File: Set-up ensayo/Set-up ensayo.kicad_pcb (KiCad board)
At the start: 2 copper layers, 14 parts, among them J1 Conn_Coaxial, J2 DB9_Female_MountingHoles

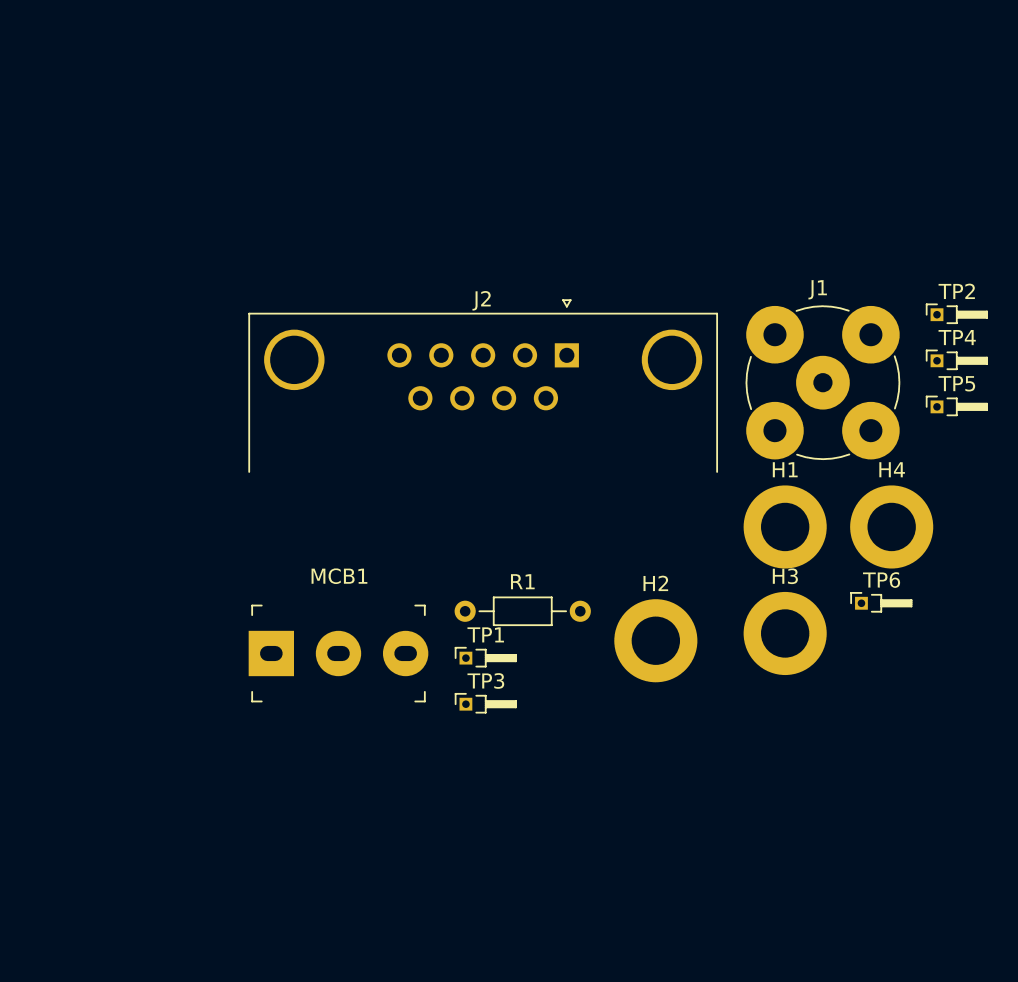
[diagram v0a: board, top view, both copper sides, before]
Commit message: Agregado de footprint de potenciómetro a PCB
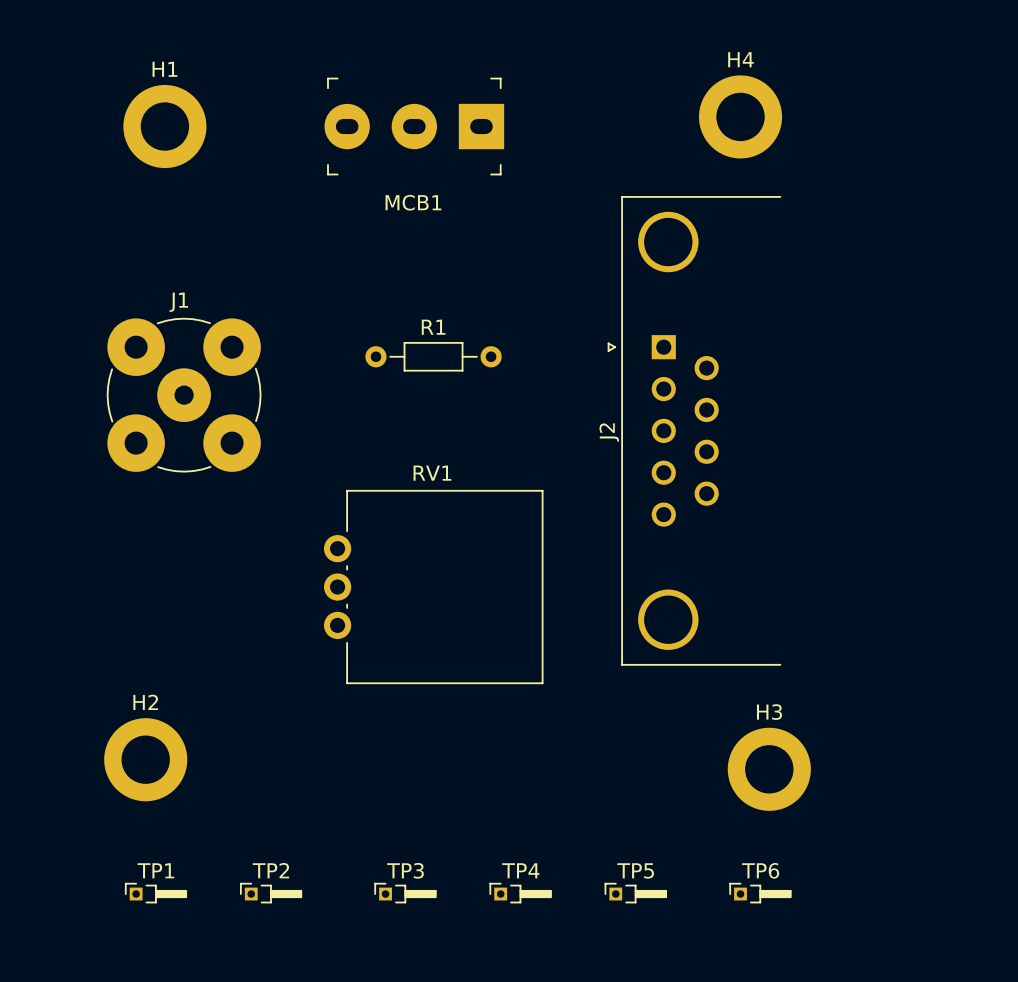
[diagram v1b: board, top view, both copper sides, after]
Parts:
- added RV1: R_POT, Footprints proyecto:Potentiometer_Vishay_248GJ-249GJ_Single_Vertical, F.Cu at (116.8, 114.3)
- moved TP2 59.4 mm to (111.1, 132.1)
- moved H1 48.9 mm to (105.4, 81.3)
- moved TP4 45.6 mm to (127.6, 132.1)
- moved J1 42.3 mm to (106.7, 99.1)
- moved TP5 38.6 mm to (135.3, 132.1)
- moved MCB1 35.2 mm to (121.9, 81.3), turned to 180 degrees
- moved H2 34.7 mm to (104.1, 123.2)
- moved H4 28.9 mm to (143.5, 80.6)
- moved TP1 26.8 mm to (103.5, 132.1)
- moved TP6 20.8 mm to (143.5, 132.1)
- moved R1 17.9 mm to (119.4, 96.5)
- moved TP3 13.6 mm to (120.0, 132.1)
- moved H3 9.05 mm to (145.4, 123.8)
- moved J2 6.44 mm to (138.4, 95.9), turned to 90 degrees

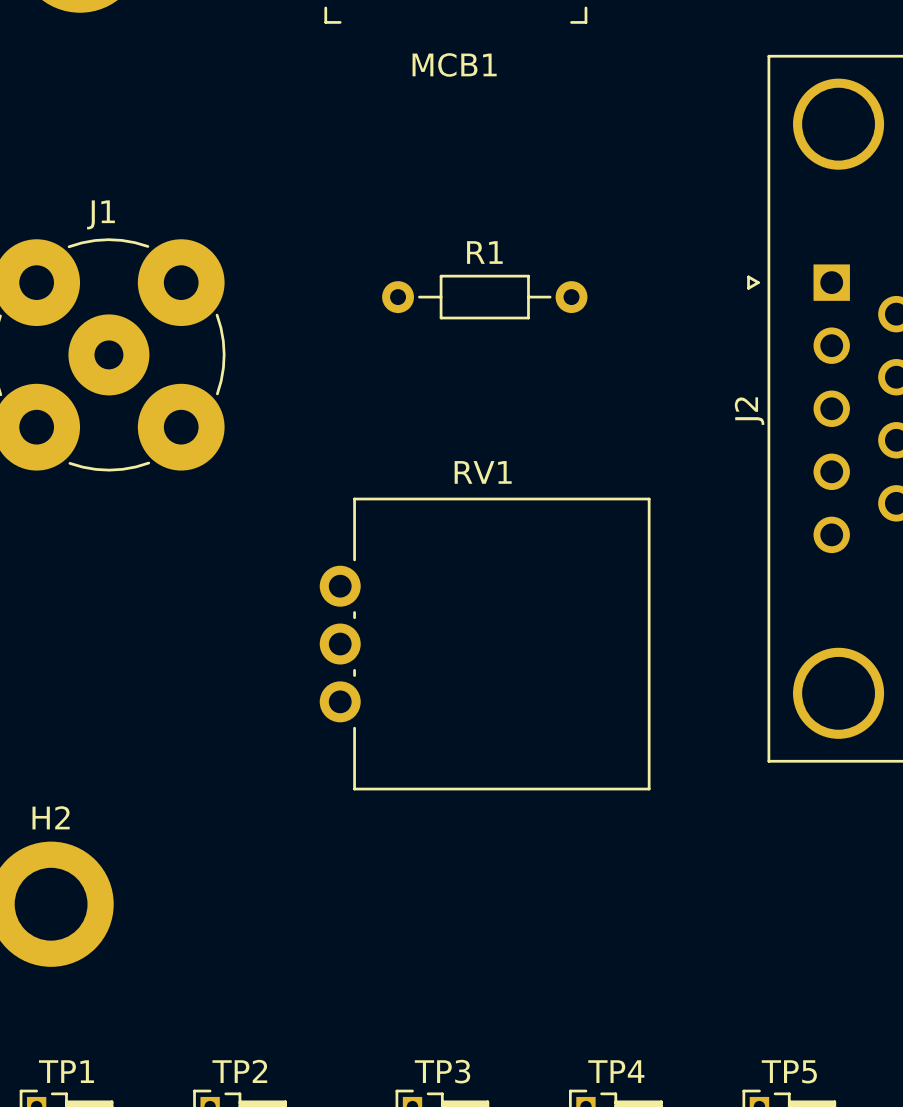
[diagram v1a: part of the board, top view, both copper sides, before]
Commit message: Agregué los nuevos componentes importados desde el esquemático
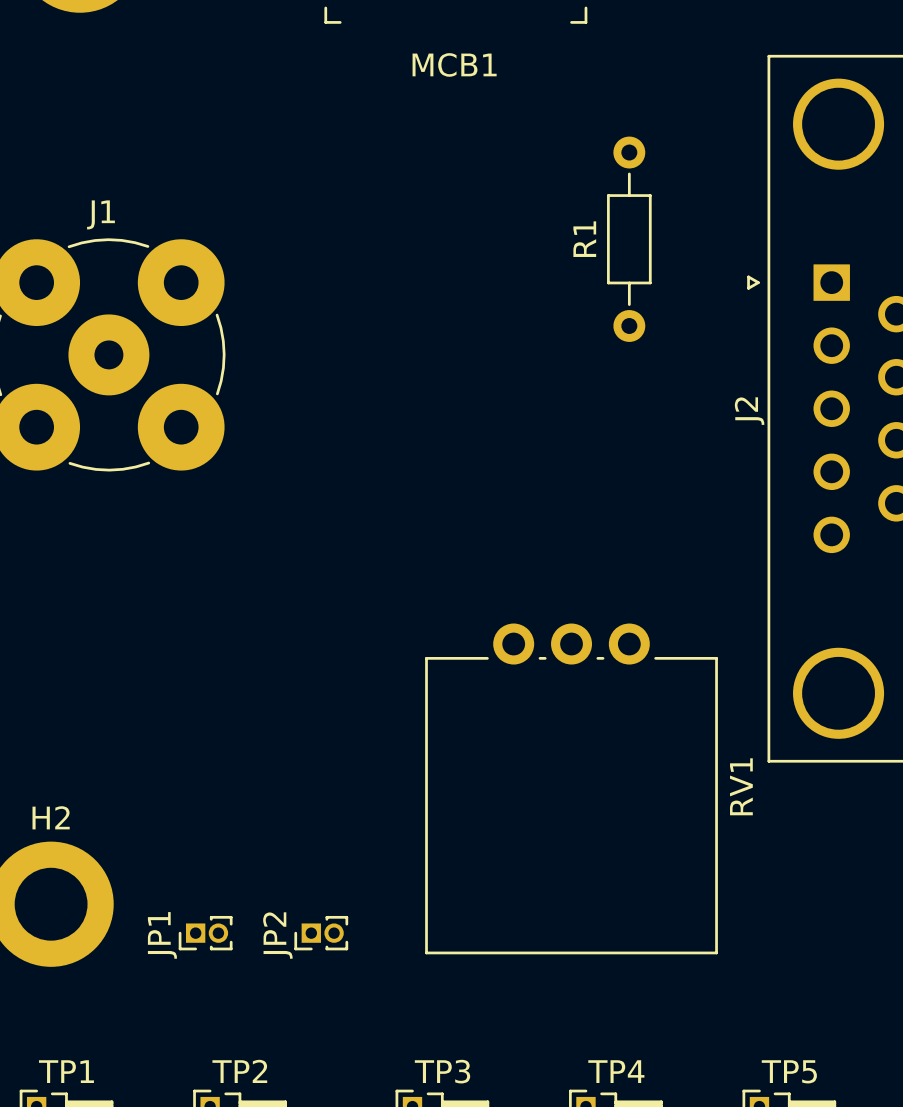
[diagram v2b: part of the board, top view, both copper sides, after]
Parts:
- added JP1: Jumper_NC_Small, Footprints proyecto:PinHeader_1x02_P1.00mm_Vertical, F.Cu at (110.5, 124.5)
- added JP2: Jumper_NO_Small, Footprints proyecto:PinHeader_1x02_P1.00mm_Vertical, F.Cu at (115.6, 124.5)
- moved R1 10.2 mm to (129.5, 97.8), turned to 90 degrees
- moved RV1 8.03 mm to (124.5, 111.8), turned to 270 degrees
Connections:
- R1 pad 1: /Vi -> Net-(JP1-Pad2)
- RV1 pad 1: /Vi -> Net-(JP2-Pad2)
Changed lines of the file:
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@@
     (tracks 0)
     (zones 0)
-    (modules 15)
-    (nets 13)
+    (modules 17)
+    (nets 15)
   )
   (page A4)
@@
   (net 11 /Vi)
   (net 12 "Net-(MCB1-Pad3)")
+  (net 13 "Net-(JP1-Pad2)")
+  (net 14 "Net-(JP2-Pad2)")
   (net_class Default "This is the default net class."
     (clearance 0.2)
@@
     (add_net "Net-(J2-Pad8)")
     (add_net "Net-(J2-Pad9)")
+    (add_net "Net-(JP1-Pad2)")
+    (add_net "Net-(JP2-Pad2)")
     (add_net "Net-(MCB1-Pad3)")
   )
+  (module "Footprints proyecto:PinHeader_1x02_P1.00mm_Vertical" (layer F.Cu)
+    (at 115.57 124.46 90)
+    (descr "Through hole straight pin header, 1x02, 1.00mm pitch, single row")
+    (tags "Through hole pin header THT 1x02 1.00mm single row")
+    (fp_text reference JP2 (at 0 -1.56 90) (layer F.SilkS)
+      (effects (font (size 1 1) (thickness 0.15)))
+    )
+    (fp_text value Jumper_NO_Small (at 0 2.56 90) (layer F.Fab)
+      (effects (font (size 1 1) (thickness 0.15)))
+    )
+    (fp_text user %R (at 0 0.5) (layer F.Fab)
+      (effects (font (size 0.76 0.76) (thickness 0.114)))
+    )
+    (fp_line (start 1.15 -1) (end -1.15 -1) (layer F.CrtYd) (width 0.05))
+    (fp_line (start 1.15 2) (end 1.15 -1) (layer F.CrtYd) (width 0.05))
+    (fp_line (start -1.15 2) (end 1.15 2) (layer F.CrtYd) (width 0.05))
+    (fp_line (start -1.15 -1) (end -1.15 2) (layer F.CrtYd) (width 0.05))
+    (fp_line (start -0.695 -0.685) (end 0 -0.685) (layer F.SilkS) (width 0.12))
+    (fp_line (start -0.695 0) (end -0.695 -0.685) (layer F.SilkS) (width 0.12))
+    (fp_line (start 0.608276 0.685) (end 0.695 0.685) (layer F.SilkS) (width 0.12))
+    (fp_line (start -0.695 0.685) (end -0.608276 0.685) (layer F.SilkS) (width 0.12))
+    (fp_line (start 0.695 0.685) (end 0.695 1.56) (layer F.SilkS) (width 0.12))
+    (fp_line (start -0.695 0.685) (end -0.695 1.56) (layer F.SilkS) (width 0.12))
+    (fp_line (start 0.394493 1.56) (end 0.695 1.56) (layer F.SilkS) (width 0.12))
+    (fp_line (start -0.695 1.56) (end -0.394493 1.56) (layer F.SilkS) (width 0.12))
+    (fp_line (start -0.635 -0.1825) (end -0.3175 -0.5) (layer F.Fab) (width 0.1))
+    (fp_line (start -0.635 1.5) (end -0.635 -0.1825) (layer F.Fab) (width 0.1))
+    (fp_line (start 0.635 1.5) (end -0.635 1.5) (layer F.Fab) (width 0.1))
+    (fp_line (start 0.635 -0.5) (end 0.635 1.5) (layer F.Fab) (width 0.1))
+    (fp_line (start -0.3175 -0.5) (end 0.635 -0.5) (layer F.Fab) (width 0.1))
+    (pad 2 thru_hole oval (at 0 1 90) (size 0.85 0.85) (drill 0.5) (layers *.Cu *.Mask)
+      (net 14 "Net-(JP2-Pad2)"))
+    (pad 1 thru_hole rect (at 0 0 90) (size 0.85 0.85) (drill 0.5) (layers *.Cu *.Mask)
+      (net 11 /Vi))
+    (model ${KISYS3DMOD}/Connector_PinHeader_1.00mm.3dshapes/PinHeader_1x02_P1.00mm_Vertical.wrl
+      (at (xyz 0 0 0))
+      (scale (xyz 1 1 1))
+      (rotate (xyz 0 0 0))
+    )
+  )
+  (module "Footprints proyecto:PinHeader_1x02_P1.00mm_Vertical" (layer F.Cu)
+    (at 110.49 124.46 90)
+    (descr "Through hole straight pin header, 1x02, 1.00mm pitch, single row")
+    (tags "Through hole pin header THT 1x02 1.00mm single row")
+    (fp_text reference JP1 (at 0 -1.56 90) (layer F.SilkS)
+      (effects (font (size 1 1) (thickness 0.15)))
+    )
+    (fp_text value Jumper_NC_Small (at 0 2.56 90) (layer F.Fab)
+      (effects (font (size 1 1) (thickness 0.15)))
+    )
+    (fp_text user %R (at 0 0.5) (layer F.Fab)
+      (effects (font (size 0.76 0.76) (thickness 0.114)))
+    )
+    (fp_line (start 1.15 -1) (end -1.15 -1) (layer F.CrtYd) (width 0.05))
+    (fp_line (start 1.15 2) (end 1.15 -1) (layer F.CrtYd) (width 0.05))
+    (fp_line (start -1.15 2) (end 1.15 2) (layer F.CrtYd) (width 0.05))
+    (fp_line (start -1.15 -1) (end -1.15 2) (layer F.CrtYd) (width 0.05))
+    (fp_line (start -0.695 -0.685) (end 0 -0.685) (layer F.SilkS) (width 0.12))
+    (fp_line (start -0.695 0) (end -0.695 -0.685) (layer F.SilkS) (width 0.12))
+    (fp_line (start 0.608276 0.685) (end 0.695 0.685) (layer F.SilkS) (width 0.12))
+    (fp_line (start -0.695 0.685) (end -0.608276 0.685) (layer F.SilkS) (width 0.12))
+    (fp_line (start 0.695 0.685) (end 0.695 1.56) (layer F.SilkS) (width 0.12))
+    (fp_line (start -0.695 0.685) (end -0.695 1.56) (layer F.SilkS) (width 0.12))
+    (fp_line (start 0.394493 1.56) (end 0.695 1.56) (layer F.SilkS) (width 0.12))
+    (fp_line (start -0.695 1.56) (end -0.394493 1.56) (layer F.SilkS) (width 0.12))
+    (fp_line (start -0.635 -0.1825) (end -0.3175 -0.5) (layer F.Fab) (width 0.1))
+    (fp_line (start -0.635 1.5) (end -0.635 -0.1825) (layer F.Fab) (width 0.1))
+    (fp_line (start 0.635 1.5) (end -0.635 1.5) (layer F.Fab) (width 0.1))
+    (fp_line (start 0.635 -0.5) (end 0.635 1.5) (layer F.Fab) (width 0.1))
+    (fp_line (start -0.3175 -0.5) (end 0.635 -0.5) (layer F.Fab) (width 0.1))
+    (pad 2 thru_hole oval (at 0 1 90) (size 0.85 0.85) (drill 0.5) (layers *.Cu *.Mask)
+      (net 13 "Net-(JP1-Pad2)"))
+    (pad 1 thru_hole rect (at 0 0 90) (size 0.85 0.85) (drill 0.5) (layers *.Cu *.Mask)
+      (net 11 /Vi))
+    (model ${KISYS3DMOD}/Connector_PinHeader_1.00mm.3dshapes/PinHeader_1x02_P1.00mm_Vertical.wrl
+      (at (xyz 0 0 0))
+      (scale (xyz 1 1 1))
+      (rotate (xyz 0 0 0))
+    )
+  )
   (module "Footprints proyecto:Potentiometer_Vishay_248GJ-249GJ_Single_Vertical" (layer F.Cu)
-    (at 116.84 114.3)
+    (at 124.46 111.76 270)
     (descr "Potentiometer, vertical, Vishay 248GJ-249GJ Single, http://www.vishay.com/docs/57054/248249.pdf")
     (tags "Potentiometer vertical Vishay 248GJ-249GJ Single")
-    (fp_text reference RV1 (at 6.275 -10.04) (layer F.SilkS)
-      (effects (font (size 1 1) (thickness 0.15)))
-    )
-    (fp_text value R_POT (at 6.275 4.96) (layer F.Fab)
-      (effects (font (size 1 1) (thickness 0.15)))
-    )
-    (fp_text user %R (at 1.75 -2.54 90) (layer F.Fab)
+    (fp_text reference RV1 (at 6.275 -10.04 90) (layer F.SilkS)
+      (effects (font (size 1 1) (thickness 0.15)))
+    )
+    (fp_text value R_POT (at 6.275 4.96 90) (layer F.Fab)
+      (effects (font (size 1 1) (thickness 0.15)))
+    )
+    (fp_text user %R (at 1.75 -2.54) (layer F.Fab)
       (effects (font (size 1 1) (thickness 0.15)))
     )
@@
     (fp_line (start 0.75 -8.79) (end 0.75 3.71) (layer F.Fab) (width 0.1))
     (fp_circle (center 7.1 -2.54) (end 10.275 -2.54) (layer F.Fab) (width 0.1))
-    (pad 1 thru_hole circle (at 0 0) (size 1.8 1.8) (drill 1) (layers *.Cu *.Mask)
-      (net 11 /Vi))
-    (pad 2 thru_hole circle (at 0 -2.54) (size 1.8 1.8) (drill 1) (layers *.Cu *.Mask)
+    (pad 1 thru_hole circle (at 0 0 270) (size 1.8 1.8) (drill 1) (layers *.Cu *.Mask)
+      (net 14 "Net-(JP2-Pad2)"))
+    (pad 2 thru_hole circle (at 0 -2.54 270) (size 1.8 1.8) (drill 1) (layers *.Cu *.Mask)
       (net 4 /VZs1))
-    (pad 3 thru_hole circle (at 0 -5.08) (size 1.8 1.8) (drill 1) (layers *.Cu *.Mask)
+    (pad 3 thru_hole circle (at 0 -5.08 270) (size 1.8 1.8) (drill 1) (layers *.Cu *.Mask)
       (net 4 /VZs1))
     (model ${KISYS3DMOD}/Potentiometer_THT.3dshapes/Potentiometer_Vishay_248GJ-249GJ_Single_Vertical.wrl
@@
   )
   (module "Footprints proyecto:R_Axial_DIN0204_L3.6mm_D1.6mm_P7.62mm_Horizontal" (layer F.Cu)
-    (at 119.38 96.52)
+    (at 129.54 97.79 90)
     (descr "Resistor, Axial_DIN0204 series, Axial, Horizontal, pin pitch=7.62mm, 0.167W, length*diameter=3.6*1.6mm^2, http://cdn-reichelt.de/documents/datenblatt/B400/1_4W%23YAG.pdf")
     (tags "Resistor Axial_DIN0204 series Axial Horizontal pin pitch 7.62mm 0.167W length 3.6mm diameter 1.6mm")
-    (fp_text reference R1 (at 3.81 -1.92) (layer F.SilkS)
-      (effects (font (size 1 1) (thickness 0.15)))
-    )
-    (fp_text value 15k (at 3.81 1.92) (layer F.Fab)
+    (fp_text reference R1 (at 3.81 -1.92 90) (layer F.SilkS)
+      (effects (font (size 1 1) (thickness 0.15)))
+    )
+    (fp_text value 15k (at 3.81 1.92 90) (layer F.Fab)
       (effects (font (size 1 1) (thickness 0.15)))
     )
@@
     (fp_line (start 8.57 1.05) (end 8.57 -1.05) (layer F.CrtYd) (width 0.05))
     (fp_line (start 8.57 -1.05) (end -0.95 -1.05) (layer F.CrtYd) (width 0.05))
-    (fp_text user %R (at 3.81 0) (layer F.Fab)
+    (fp_text user %R (at 3.81 0 90) (layer F.Fab)
       (effects (font (size 0.72 0.72) (thickness 0.108)))
     )
-    (pad 1 thru_hole circle (at 0 0) (size 1.4 1.4) (drill 0.7) (layers *.Cu *.Mask)
-      (net 11 /Vi))
-    (pad 2 thru_hole oval (at 7.62 0) (size 1.4 1.4) (drill 0.7) (layers *.Cu *.Mask)
+    (pad 1 thru_hole circle (at 0 0 90) (size 1.4 1.4) (drill 0.7) (layers *.Cu *.Mask)
+      (net 13 "Net-(JP1-Pad2)"))
+    (pad 2 thru_hole oval (at 7.62 0 90) (size 1.4 1.4) (drill 0.7) (layers *.Cu *.Mask)
       (net 4 /VZs1))
     (model ${KISYS3DMOD}/Resistor_THT.3dshapes/R_Axial_DIN0204_L3.6mm_D1.6mm_P7.62mm_Horizontal.wrl

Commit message: Terminé con paso 1 de proceso de diseño de PCB, quedaron revisadas las reglas de diseño de PCB
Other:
- net class Señal added: clearance 0.2, trace_width 1, via_dia 0.8, via_drill 0.4
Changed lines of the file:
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@@
+    (uvia_dia 0.3)
+    (uvia_drill 0.1)
+    (add_net "Net-(MCB1-Pad3)")
+  )
+  (net_class Señal ""
+    (clearance 0.2)
+    (trace_width 1)
+    (via_dia 0.8)
+    (via_drill 0.4)
     (uvia_dia 0.3)
     (uvia_drill 0.1)
@@
     (add_net "Net-(JP1-Pad2)")
     (add_net "Net-(JP2-Pad2)")
-    (add_net "Net-(MCB1-Pad3)")
   )
   (module "Footprints proyecto:PinHeader_1x02_P1.00mm_Vertical" (layer F.Cu)
